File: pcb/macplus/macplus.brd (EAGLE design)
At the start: 54 x 32 mm, 11 parts, among them J1 ATX24RH

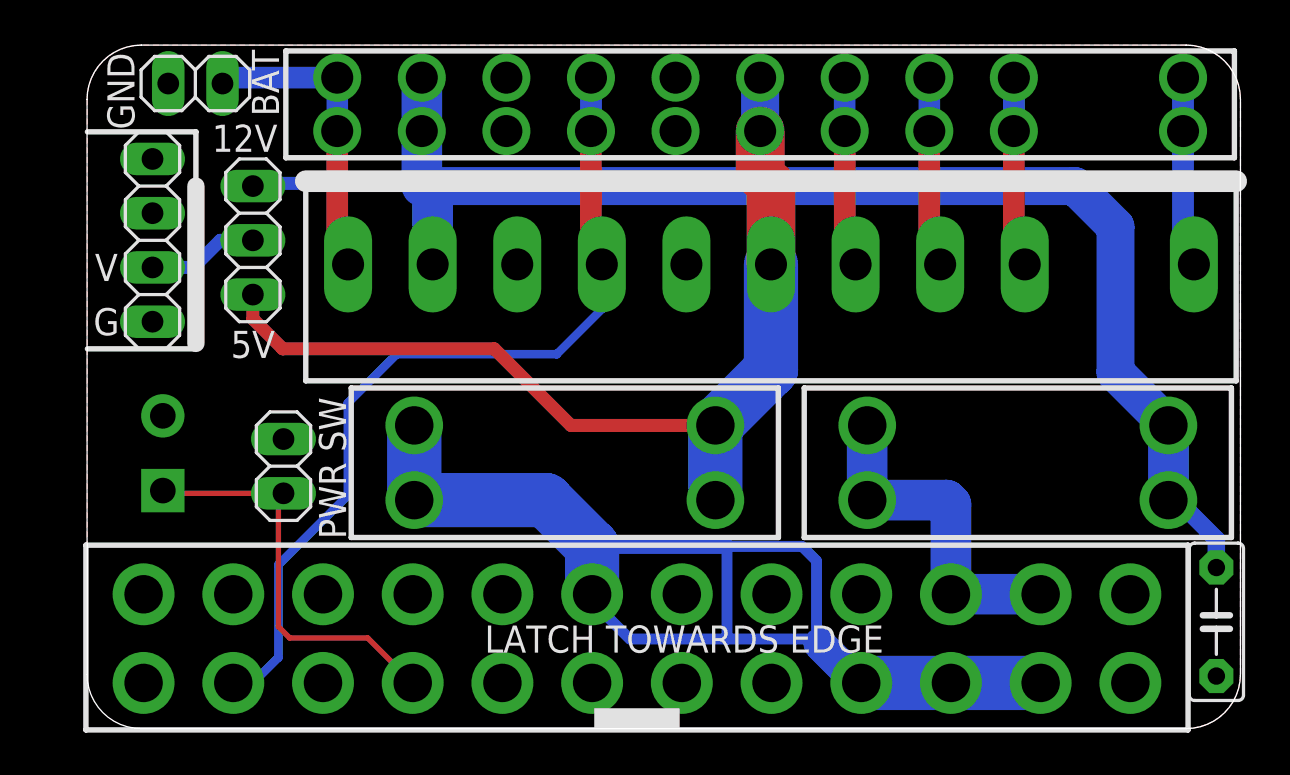
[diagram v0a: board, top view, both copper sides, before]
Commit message: BBC micro USB adaptor
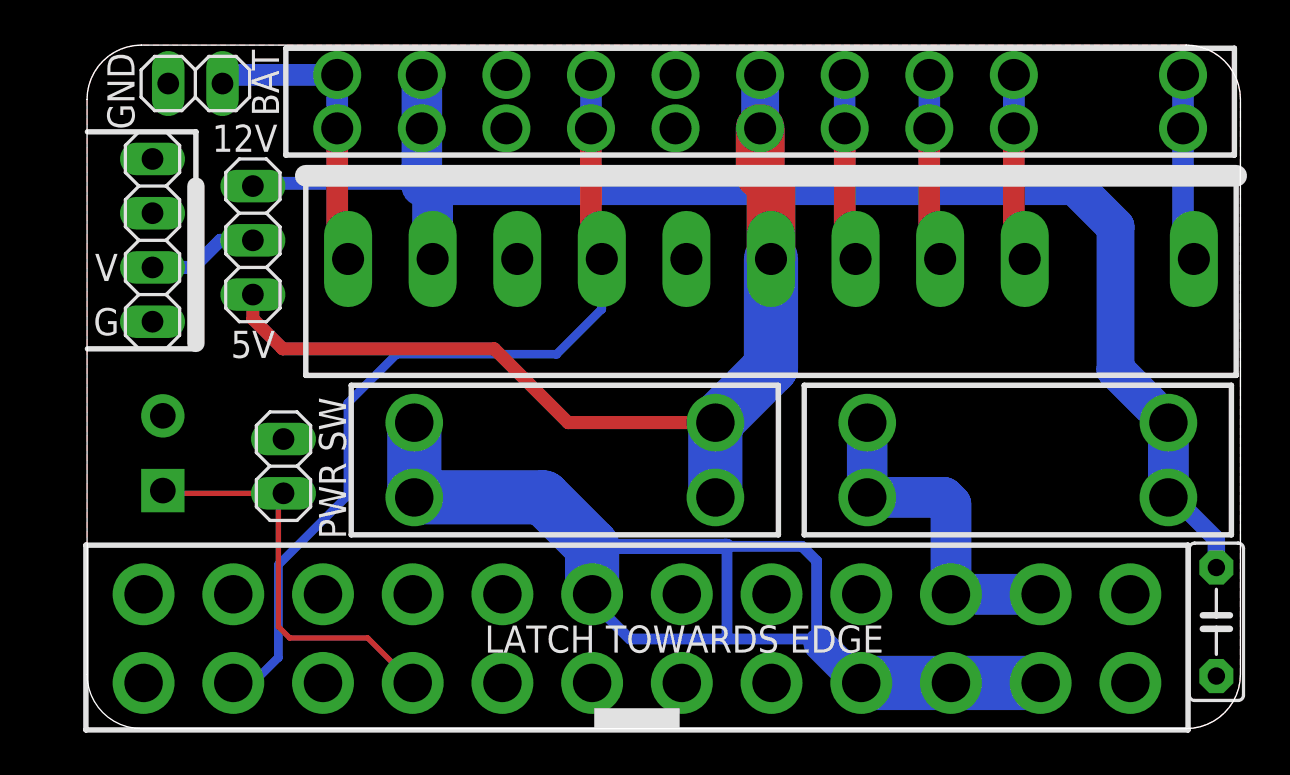
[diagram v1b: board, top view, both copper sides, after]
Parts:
- moved U$1 0.25 mm to (33.0, 22.0)
- moved U$3 0.13 mm to (32.5, 29.4)
- moved U$2 0.13 mm to (44.6, 12.6)
- moved U$8 0.13 mm to (23.4, 12.6)
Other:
- board text added: "dekuNukem PD3 APR23"
- board text removed: "dekuNukem PD2 Dec22"

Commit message: updated with more caps
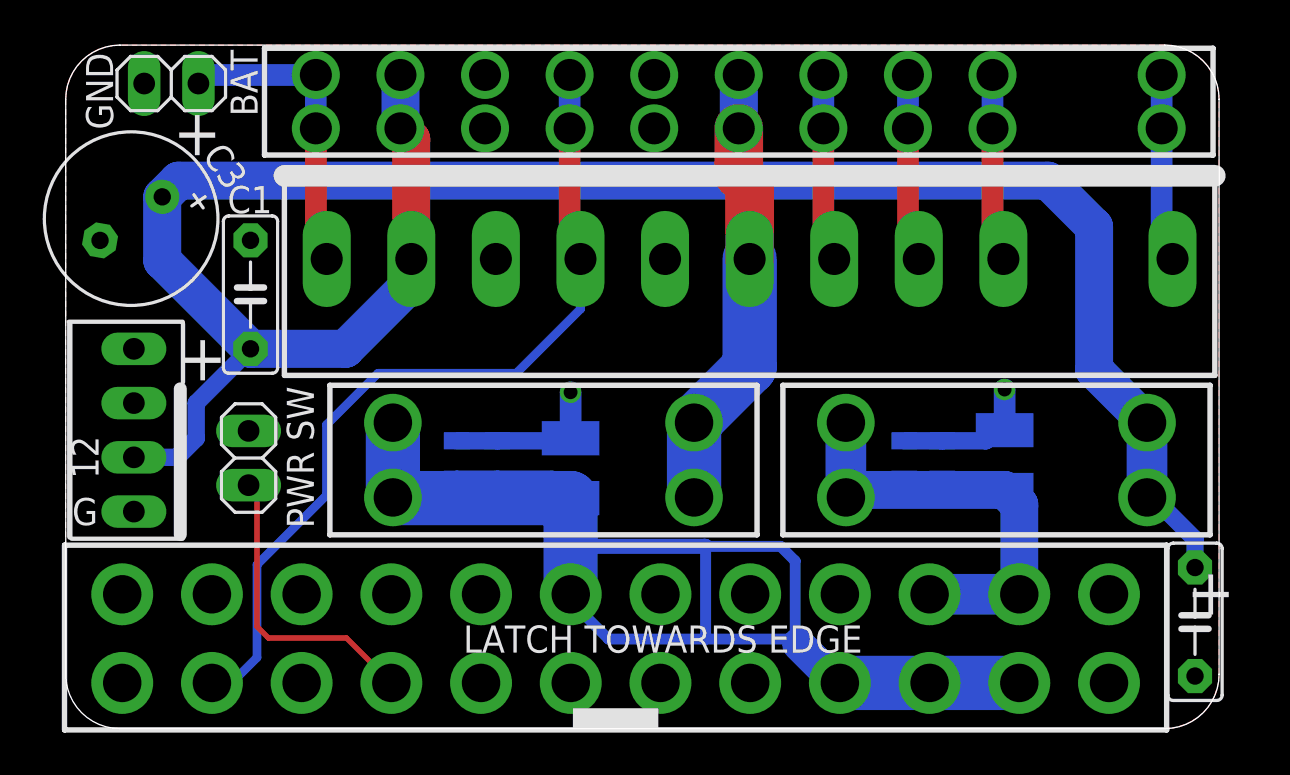
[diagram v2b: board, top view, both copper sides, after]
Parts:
- removed J7: (no value), atx_power_control:SCREWTERMINAL-3.5MM-2-NS
- removed JP4: (no value), atx_power_control:1X04
- added C1: (no value), capacitor-wima:C5B2.5
- added C12, C5, C6, C7: 100nF, clock:0805@1
- added C3: (no value), adafruit_changed:E3,5-8
- added C4, C8: 47uF, clock:C1210
- JP1: device pinhead:1X03 -> appleii:1X04
- moved JP1 10.5 mm to (3.19, 14.0)
- moved JP2 1.68 mm to (8.56, 12.7)
- moved JP3 1.13 mm to (4.94, 30.2)
- moved C2 1.00 mm to (52.9, 5.00)
- moved J1 1.00 mm to (25.7, 4.24)
- moved U$1 1.00 mm to (32.0, 22.0)
- moved U$2 1.00 mm to (43.6, 12.6)
- moved U$3 1.00 mm to (31.5, 29.4)
- moved U$8 1.00 mm to (22.4, 12.6)
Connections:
- removed net N$7: JP1.2, JP4.3
- net +12V: now also C1.1, C3.+, JP1.2; no longer JP1.3
- net +5V: no longer JP1.1
- net GND: now also C1.2, C12.1, C3.-, C4.2, C5.1, C6.1, C7.1, C8.2, JP1.1; no longer J7.2, JP4.4
- net N$5: no longer J7.1
- net N$6: now also C12.2, C7.2, C8.1
- net N$8: now also C4.1, C5.2, C6.2
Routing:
- net +12V: track 68.5 -> 99.0 mm
- net +5V: track 45.9 -> 21.1 mm
- net N$6: track 56.8 -> 71.7 mm
- net GND: track 0.00 -> 14.7 mm, vias 0 -> 2
- net N$8: track 16.0 -> 25.3 mm
- net N$5: track 19.4 -> 14.2 mm
- net N$7: track 5.23 -> 0.00 mm
- net -12V: track 40.8 -> 40.2 mm
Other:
- board text added: "12"
- board text added: "Mac 128K/Plus PicoPSU Adaptor"
- board text added: "USE 5A FUSE"
- board text added: "picoRC.com"
- board text removed: "12V"
- board text removed: "5V"
- board text removed: "FUSE 5A MAX"
- board text removed: "Instructions picoRC.com"
- board text removed: "Mac 128K/512K/Plus PicoPSU Adaptor"
- board text removed: "V"
- board text removed: "dekuNukem PD3 APR23"

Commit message: adjusted footprint
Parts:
- moved JP1 0.89 mm to (3.19, 14.9)
- moved C3 0.63 mm to (3.06, 24.5)
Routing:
- net N$6: track 71.7 -> 86.0 mm
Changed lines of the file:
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@@
 <text x="16.399" y="25.4" size="1.27" layer="26" rot="MR180" align="center">+12</text>
 <text x="12.081" y="25.4" size="1.27" layer="26" rot="MR180" align="center">BAT</text>
-<text x="0.905" y="12.7" size="1.27" layer="25" rot="R90" align="center">12</text>
+<text x="0.905" y="13.589" size="1.27" layer="25" rot="R90" align="center">12</text>
 <text x="47.895" y="25.527" size="1.778" layer="26" distance="30" rot="MR270" align="center">picoRC.com</text>
-<text x="53.61" y="6.4308" size="2.1844" layer="25" rot="R180" align="center">+</text>
+<text x="53.483" y="6.5578" size="1.27" layer="25" rot="R180" align="center">+</text>
 <text x="32.909" y="12.573" size="1.778" layer="26" distance="30" rot="MR270" align="center">USE 5A
 FUSE</text>
 <text x="10.9842" y="12.7" size="1.27" layer="25" rot="R270" align="center">PWR SW</text>
-<text x="6.1582" y="27.94" size="2.1844" layer="25" rot="MR0" align="center">+</text>
-<text x="0.905" y="10.16" size="1.27" layer="25" align="center">G</text>
-<text x="6.4122" y="17.399" size="2.1844" layer="25" rot="MR0" align="center">+</text>
+<text x="6.6662" y="27.94" size="2.1844" layer="25" rot="MR0" align="center">+</text>
+<text x="0.905" y="11.049" size="1.27" layer="25" align="center">G</text>
+<text x="6.5392" y="18.034" size="2.1844" layer="25" rot="MR0" align="center">+</text>
 </plain>
 <attributes>
@@
 <attribute name="VALUE" x="50.079" y="7.032" size="1.27" layer="27" ratio="10" rot="R270"/>
 </element>
-<element name="JP1" library="appleii" package="1X04" value="" x="3.191" y="13.97" smashed="yes" rot="R90"/>
+<element name="JP1" library="appleii" package="1X04" value="" x="3.191" y="14.859" smashed="yes" rot="R90"/>
 <element name="C1" library="capacitor-wima" library_urn="urn:adsk.eagle:library:116" package="C5B2.5" package3d_urn="urn:adsk.eagle:package:5426/1" value="" x="8.652" y="20.32" smashed="yes" rot="R90">
 <attribute name="NAME" x="9.668" y="25.4" size="1.27" layer="25" ratio="10" rot="R180"/>
@@
 <attribute name="VALUE" x="11.446" y="18.288" size="1.27" layer="27" ratio="10" rot="R90"/>
 </element>
-<element name="C3" library="adafruit_changed" package="E3,5-8" value="" x="3.064" y="23.876" smashed="yes" rot="R215">
-<attribute name="NAME" x="6.3576625" y="26.837728125" size="1.27" layer="25" ratio="10" rot="R305"/>
-<attribute name="VALUE" x="3.18831875" y="27.68396875" size="1.27" layer="27" ratio="10" rot="R215"/>
+<element name="C3" library="adafruit_changed" package="E3,5-8" value="" x="3.064" y="24.511" smashed="yes" rot="R215">
+<attribute name="NAME" x="1.9126625" y="21.884728125" size="1.27" layer="25" ratio="10" rot="R305"/>
+<attribute name="VALUE" x="3.18831875" y="28.31896875" size="1.27" layer="27" ratio="10" rot="R215"/>
 </element>
 <element name="C8" library="clock" package="C1210" value="47uF" x="23.638" y="12.192" smashed="yes" rot="MR90">
@@
 <wire x1="23.638" y1="10.792" x2="23.646" y2="10.784" width="0.8128" layer="16"/>
 <wire x1="23.646" y1="10.784" x2="23.646" y2="6.288" width="0.8128" layer="16"/>
+<wire x1="36.246" y1="2.138" x2="34.193" y2="4.191" width="0.508" layer="1"/>
+<wire x1="25.743" y1="4.191" x2="23.646" y2="6.288" width="0.508" layer="1"/>
+<wire x1="34.193" y1="4.191" x2="25.743" y2="4.191" width="0.508" layer="1"/>
 </signal>
 <signal name="N$8">
@@
 <wire x1="15.672" y1="28.103" x2="16.18" y2="27.595" width="1.778" layer="1"/>
 <wire x1="16.18" y1="27.595" x2="16.18" y2="21.987" width="1.778" layer="1"/>
-<wire x1="45.99" y1="25.654" x2="5.27863125" y2="25.654" width="1.778" layer="16"/>
-<wire x1="5.27863125" y1="25.654" x2="4.52045" y2="24.89581875" width="1.778" layer="16"/>
-<wire x1="4.52045" y1="24.89581875" x2="4.52045" y2="21.91155" width="1.778" layer="16"/>
+<wire x1="45.99" y1="25.654" x2="4.64363125" y2="25.654" width="1.778" layer="16"/>
+<wire x1="4.64363125" y1="25.654" x2="4.52045" y2="25.53081875" width="1.778" layer="16"/>
+<wire x1="4.52045" y1="25.53081875" x2="4.52045" y2="21.91155" width="1.778" layer="16"/>
 <wire x1="4.52045" y1="21.91155" x2="8.652" y2="17.78" width="1.778" layer="16"/>
 <wire x1="8.652" y1="17.78" x2="6.112" y2="15.24" width="0.8128" layer="16"/>
-<wire x1="5.223" y1="12.7" x2="3.191" y2="12.7" width="0.8128" layer="16"/>
+<wire x1="6.112" y1="13.589" x2="3.191" y2="13.589" width="0.8128" layer="16"/>
 <wire x1="6.112" y1="15.24" x2="6.112" y2="13.589" width="0.8128" layer="16"/>
-<wire x1="6.112" y1="13.589" x2="5.223" y2="12.7" width="0.8128" layer="16"/>
 </signal>
 <signal name="N$5">

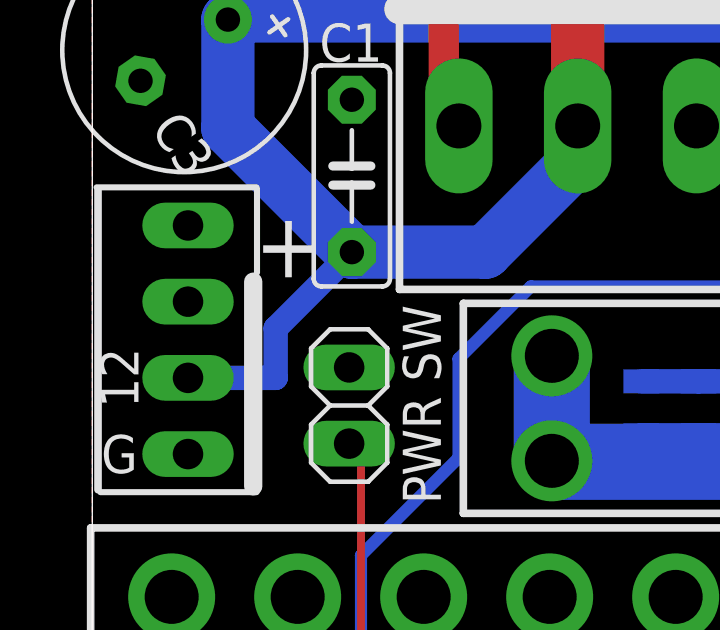
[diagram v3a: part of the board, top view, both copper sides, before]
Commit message: trace cleanup
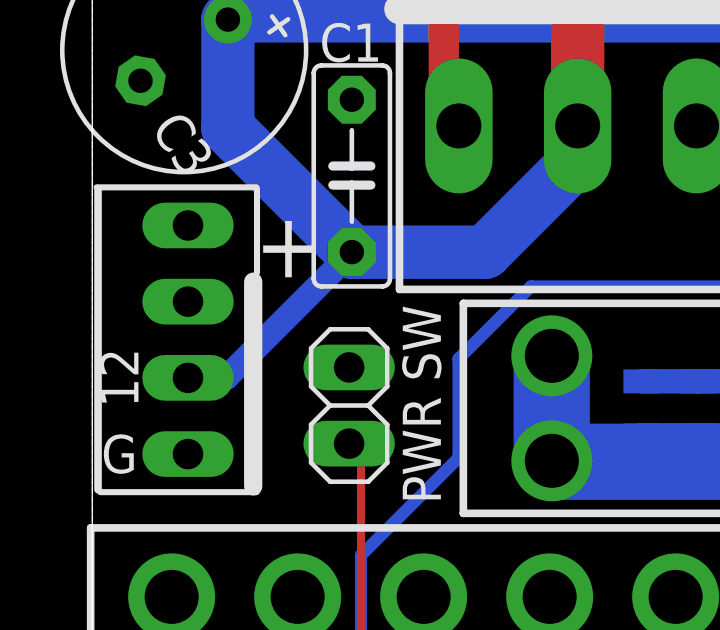
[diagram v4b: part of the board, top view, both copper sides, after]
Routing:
- net +12V: track 99.0 -> 98.1 mm
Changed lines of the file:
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@@
 <wire x1="4.52045" y1="25.53081875" x2="4.52045" y2="21.91155" width="1.778" layer="16"/>
 <wire x1="4.52045" y1="21.91155" x2="8.652" y2="17.78" width="1.778" layer="16"/>
-<wire x1="8.652" y1="17.78" x2="6.112" y2="15.24" width="0.8128" layer="16"/>
-<wire x1="6.112" y1="13.589" x2="3.191" y2="13.589" width="0.8128" layer="16"/>
-<wire x1="6.112" y1="15.24" x2="6.112" y2="13.589" width="0.8128" layer="16"/>
+<wire x1="4.461" y1="13.589" x2="3.191" y2="13.589" width="0.8128" layer="16"/>
+<wire x1="8.652" y1="17.78" x2="4.461" y2="13.589" width="0.8128" layer="16"/>
 </signal>
 <signal name="N$5">
